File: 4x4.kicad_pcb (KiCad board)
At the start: 2 copper layers, 76.2 x 76.2 mm, 43 parts, among them J1 Jumper, J2 Jumper, J3 Jumper, J4 Jumper, J5 Jumper, J6 Jumper, SW1 SW_PUSH, SW10 SW_PUSH, SW11 SW_PUSH, SW12 SW_PUSH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

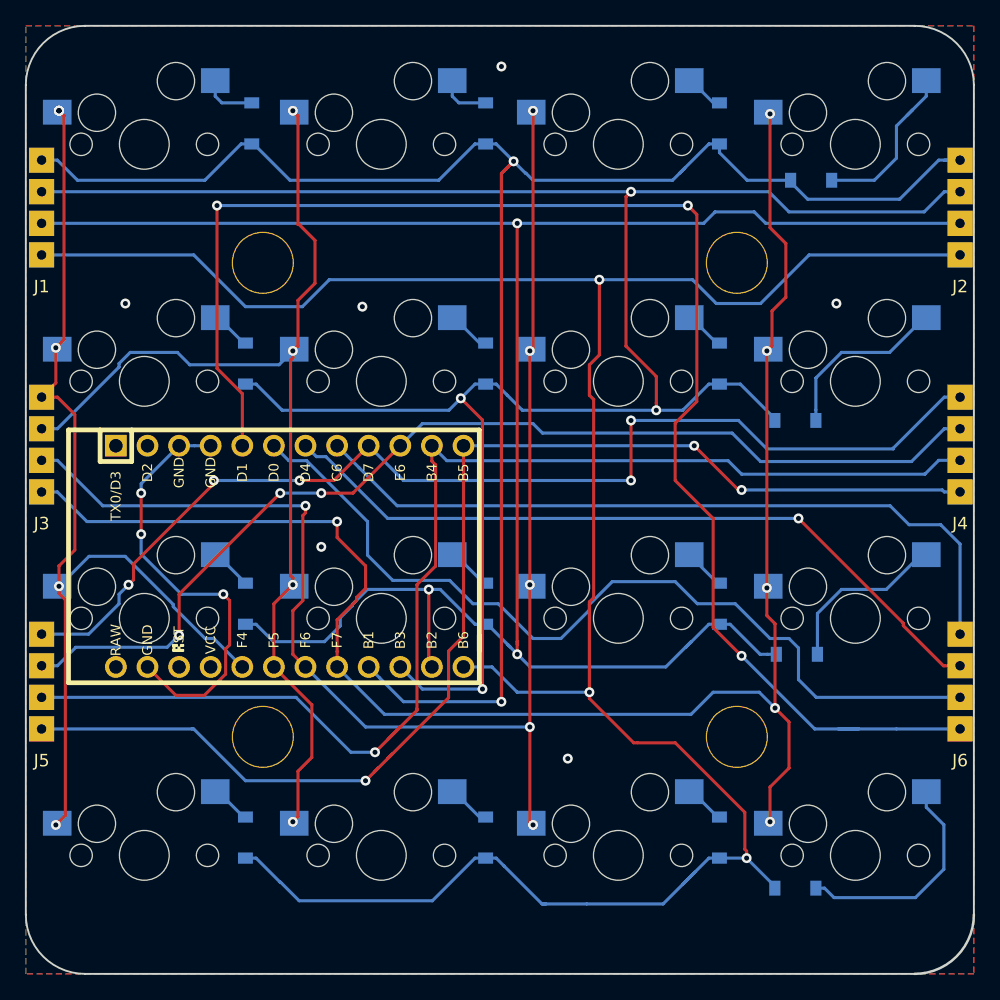
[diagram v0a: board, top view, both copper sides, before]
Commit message: フットプリントを3ピンにした
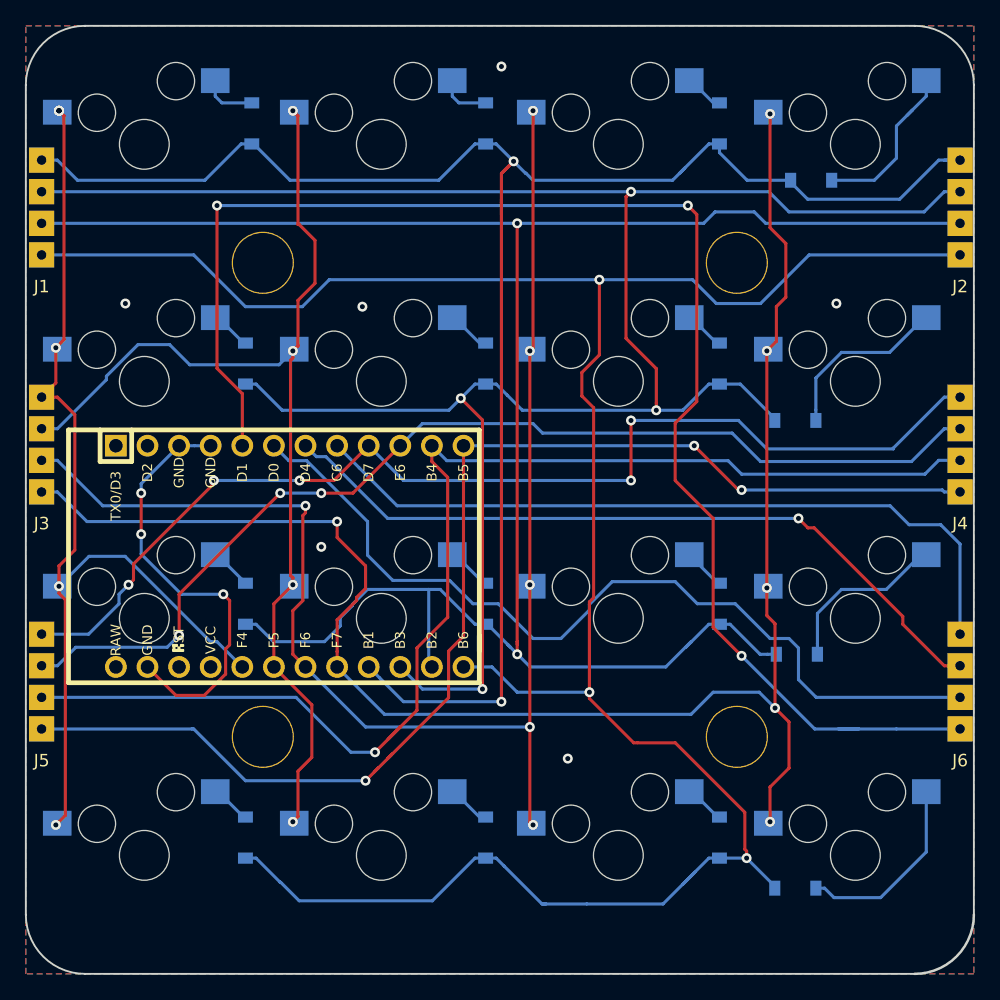
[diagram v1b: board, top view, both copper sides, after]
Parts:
- SW1, SW10, SW11, SW12, SW13, SW14, SW15, SW16, SW2, SW3, SW4, SW5, SW6, SW7, SW8, SW9: footprint lib:CherryMX_Hotswap_singleside -> lib:CherryMX_Hotswap_singleside_3pin
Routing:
- net Net-(D16-Pad2): track 18.4 -> 15.6 mm
- net col6: track 100.7 -> 101.5 mm
- net col1: track 85.1 -> 85.7 mm
- net row3: track 195.2 -> 195.8 mm
- net row2: track 167.1 -> 167.5 mm, vias 3 -> 2
